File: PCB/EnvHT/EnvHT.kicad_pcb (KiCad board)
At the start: 2 copper layers, 29.5 x 18.4 mm, 21 parts, among them J1 DC, J2 DC, J4 Shelly, U1 LMR16006XDDCR, U4 ESP32-PICO-MINI-02, U7 SHT40

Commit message: Library update
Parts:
- added C5: 10nF, RevK:C_0603, F.Cu at (88.7, 88.8)
- added S1: Screw, RevK:Screw, F.Cu at (81.0, 84.0)
- added S2: Screw, RevK:Screw, F.Cu at (124.0, 84.0)
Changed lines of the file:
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@@
   (net 39 "unconnected-(U1-Pad1)")
   (net 40 "unconnected-(U1-Pad6)")
+  (footprint "RevK:C_0603" (layer "F.Cu")
+    (at 88.7 88.75 -90)
+    (descr "Capacitor SMD 0603 (1608 Metric), square (rectangular) end terminal, IPC_7351 nominal, (Body size source: IPC-SM-782 page 76, https://www.pcb-3d.com/wordpress/wp-content/uploads/ipc-sm-782a_amendment_1_and_2.pdf), generated with kicad-footprint-generator")
+    (tags "capacitor")
+    (property "Sheetfile" "EnvHT.kicad_sch")
+    (property "Sheetname" "")
+    (attr smd)
+    (fp_text reference "C5" (at -1.6 0) (layer "F.SilkS") hide
+      (effects (font (size 0.5 0.5) (thickness 0.08)))
+    )
+    (fp_text value "10nF" (at 0 0 90) (layer "F.Fab")
+      (effects (font (size 0.4 0.4) (thickness 0.08)))
+    )
+    (fp_text user "${REFERENCE}" (at 0 -0.8 90) (layer "F.Fab")
+      (effects (font (size 0.4 0.4) (thickness 0.06)))
+    )
+    (fp_line (start -0.3 -0.5) (end 0.3 -0.5) (layer "F.SilkS") (width 0.12))
+    (fp_line (start -0.3 0.5) (end 0.3 0.5) (layer "F.SilkS") (width 0.12))
+    (fp_line (start -0.8 0.4) (end -0.8 -0.4) (layer "F.CrtYd") (width 0.05))
+    (fp_line (start -0.8 -0.4) (end 0.8 -0.4) (layer "F.CrtYd") (width 0.05))
+    (fp_line (start 0.8 0.4) (end -0.8 0.4) (layer "F.CrtYd") (width 0.05))
+    (fp_line (start 0.8 -0.4) (end 0.8 0.4) (layer "F.CrtYd") (width 0.05))
+    (fp_line (start -0.8 0.4) (end -0.8 -0.4) (layer "F.Fab") (width 0.1))
+    (fp_line (start 0.8 -0.4) (end 0.8 0.4) (layer "F.Fab") (width 0.1))
+    (fp_line (start -0.8 -0.4) (end 0.8 -0.4) (layer "F.Fab") (width 0.1))
+    (fp_line (start 0.8 0.4) (end -0.8 0.4) (layer "F.Fab") (width 0.1))
+    (pad "1" smd roundrect (at -0.775 0 270) (size 0.8 0.95) (layers "F.Cu" "F.Paste" "F.Mask") (roundrect_rratio 0.25)
+      (net 5 "GND") (pintype "passive"))
+    (pad "2" smd roundrect (at 0.775 0 270) (size 0.8 0.95) (layers "F.Cu" "F.Paste" "F.Mask") (roundrect_rratio 0.25)
+      (net 2 "Net-(R12-Pad2)") (pintype "passive"))
+    (model "${KICAD6_3DMODEL_DIR}/Capacitor_SMD.3dshapes/C_0603_1608Metric.step"
+      (offset (xyz 0 0 0))
+      (scale (xyz 1 1 1))
+      (rotate (xyz 0 0 0))
+    )
+  )
   (footprint "RevK:R_0603" (layer "F.Cu")
     (at 106.925 88.75)
@@
     )
   )
+  (footprint "RevK:Screw" (layer "F.Cu")
+    (at 81 84)
+    (property "Sheetfile" "EnvHT.kicad_sch")
+    (property "Sheetname" "")
+    (property "exclude_from_bom" "")
+    (attr exclude_from_bom)
+    (fp_text reference "S1" (at 0.15 -2.65 unlocked) (layer "F.SilkS") hide
+      (effects (font (size 1 1) (thickness 0.15)))
+    )
+    (fp_text value "Screw" (at 0.05 4 unlocked) (layer "F.Fab")
+      (effects (font (size 1 1) (thickness 0.15)))
+    )
+    (fp_line (start -3 0) (end 3 0) (layer "F.Fab") (width 1))
+    (fp_line (start 0 -3) (end 0 3) (layer "F.Fab") (width 1))
+    (fp_circle (center 0 0) (end 6 0) (layer "F.Fab") (width 0.1) (fill none))
+    (model "/Users/adrian/Documents/KiCad/3D/653612.stp"
+      (offset (xyz 0 0 5))
+      (scale (xyz 1 1 1))
+      (rotate (xyz 0 90 0))
+    )
+  )
   (footprint "RevK:C_0603_" (layer "F.Cu")
     (at 107.95 87.3)
@@
     )
   )
+  (footprint "RevK:Screw" (layer "F.Cu")
+    (at 124 84)
+    (property "Sheetfile" "EnvHT.kicad_sch")
+    (property "Sheetname" "")
+    (property "exclude_from_bom" "")
+    (attr exclude_from_bom)
+    (fp_text reference "S2" (at 0.15 -2.65 unlocked) (layer "F.SilkS") hide
+      (effects (font (size 1 1) (thickness 0.15)))
+    )
+    (fp_text value "Screw" (at 0.05 4 unlocked) (layer "F.Fab")
+      (effects (font (size 1 1) (thickness 0.15)))
+    )
+    (fp_line (start -3 0) (end 3 0) (layer "F.Fab") (width 1))
+    (fp_line (start 0 -3) (end 0 3) (layer "F.Fab") (width 1))
+    (fp_circle (center 0 0) (end 6 0) (layer "F.Fab") (width 0.1) (fill none))
+    (model "/Users/adrian/Documents/KiCad/3D/653612.stp"
+      (offset (xyz 0 0 5))
+      (scale (xyz 1 1 1))
+      (rotate (xyz 0 90 0))
+    )
+  )

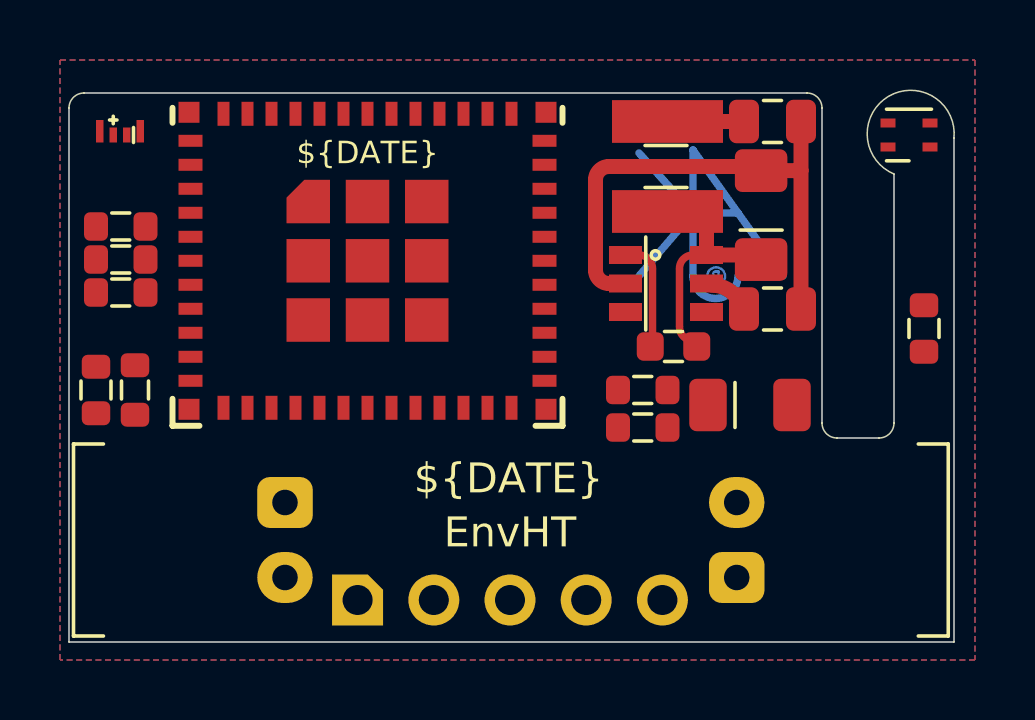
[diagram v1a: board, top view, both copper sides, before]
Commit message: Tracked EnvHT
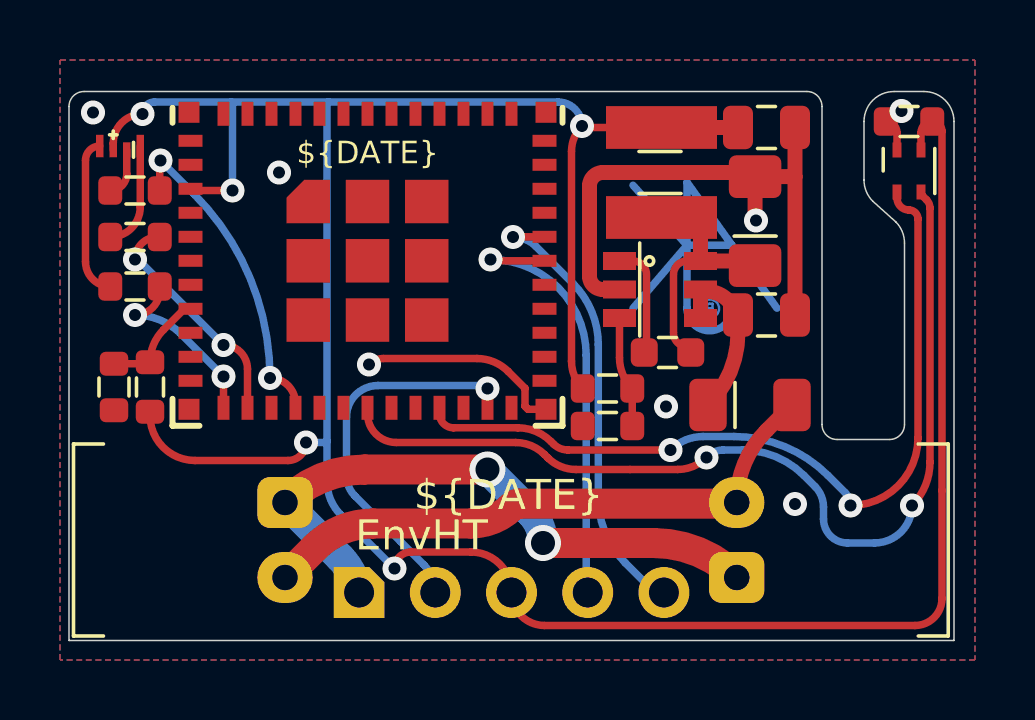
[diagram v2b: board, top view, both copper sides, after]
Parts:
- moved C4 6.92 mm to (115.8, 79.8), turned to 180 degrees
- moved R7 2.35 mm to (90.0, 82.1)
- moved U7 1.20 mm to (115.8, 81.5), turned to 90 degrees
- moved R1 1.18 mm to (105.8, 88.7)
- moved R2 1.18 mm to (105.8, 90.0)
- moved Logo1 1.09 mm to (108.4, 83.9)
- moved C5 0.61 mm to (89.3, 88.7), turned to 90 degrees
- moved R8 0.59 mm to (90.0, 83.7)
- moved R9 0.52 mm to (90.0, 85.3)
- moved R12 0.51 mm to (90.5, 88.7), turned to 90 degrees
- moved D3 0.49 mm to (89.5, 80.7)
- moved C1 0.28 mm to (107.8, 87.5)
- moved C2 0.28 mm to (111.0, 86.2)
- moved C3 0.28 mm to (111.0, 80.0)
- moved D1 0.28 mm to (110.7, 83.1)
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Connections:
- U4 pad 12: unconnected-(U4-Pad12) -> B
- U4 pad 13: unconnected-(U4-Pad13) -> G
- U4 pad 15: unconnected-(U4-Pad15) -> R
- U4 pad 18: unconnected-(U4-Pad18) -> SCL
- U4 pad 21: unconnected-(U4-Pad21) -> SDA
- U4 pad 27: G -> unconnected-(U4-Pad27)
- U4 pad 28: R -> unconnected-(U4-Pad28)
- U4 pad 33: B -> unconnected-(U4-Pad33)
- U4 pad 34: SDA -> unconnected-(U4-Pad34)
- U4 pad 35: SCL -> unconnected-(U4-Pad35)
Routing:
- net +3.3V: track 0.00 -> 94.2 mm, vias 0 -> 5
- net SCL: track 0.00 -> 32.3 mm, vias 0 -> 2
- net GND: track 0.00 -> 30.6 mm, vias 0 -> 9
- net SDA: track 0.00 -> 27.3 mm, vias 0 -> 2
- net Net-(D2-Pad2): track 0.00 -> 19.7 mm
- net O: track 0.00 -> 15.1 mm, vias 0 -> 1
- net I: track 0.00 -> 14.9 mm, vias 0 -> 1
- net BOOT: track 0.00 -> 12.9 mm, vias 0 -> 1
- net R: track 0.00 -> 10.8 mm, vias 0 -> 2
- net G: track 0.00 -> 7.86 mm, vias 0 -> 2
- net B: track 0.00 -> 6.13 mm, vias 0 -> 2
- net Net-(D3-Pad1): track 0.00 -> 5.37 mm
- net DC: track 0.00 -> 4.20 mm
- net Net-(R1-Pad2): track 0.00 -> 3.71 mm
- net Net-(C5-Pad2): track 0.00 -> 3.60 mm
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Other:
- board size 29.5 x 18.4 mm -> 29.5 x 18.3 mm

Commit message: Library update
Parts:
- moved S1 2.00 mm to (83.0, 84.0)
- moved S2 2.00 mm to (122.0, 84.0)

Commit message: Tody
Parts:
- moved S1 1.00 mm to (84.0, 84.0)
- moved S2 1.00 mm to (121.0, 84.0)
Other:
- board size 29.5 x 18.3 mm -> 29.5 x 18.2 mm
- board text added: "SDA: 15 SCL: 14"
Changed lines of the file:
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@@
     )
   )
-  (property "DATE" "2023-04-29")
+  (property "DATE" "2023-05-01")
   (net 0 "")
   (net 1 "Net-(D2-Pad2)")
@@
   )
   (footprint "RevK:Screw" (layer "F.Cu")
-    (at 83 84)
+    (at 84 84)
     (property "Sheetfile" "EnvHT.kicad_sch")
     (property "Sheetname" "")
@@
   )
   (footprint "RevK:Screw" (layer "F.Cu")
-    (at 122 84)
+    (at 121 84)
     (property "Sheetfile" "EnvHT.kicad_sch")
     (property "Sheetname" "")
@@
       (effects (font (size 0.5 0.5) (thickness 0.08)) (justify mirror))
     )
-    (fp_text user "3.3" (at -0.7 0.7 315 unlocked) (layer "B.SilkS")
-      (effects (font (size 0.7 0.7) (thickness 0.1)) (justify mirror))
-    )
     (fp_text user "3V3" (at -0.83 0.8 315 unlocked) (layer "B.SilkS")
       (effects (font (size 0.5 0.5) (thickness 0.08)) (justify mirror))
@@
       (net 20 "O") (pinfunction "Tx") (pintype "passive"))
   )
-  (gr_line (start 127.8 78) (end 77.2 78) (layer "Eco1.User") (width 0.1))
-  (gr_line (start 77.2 97.1) (end 127.8 97.1) (layer "Eco1.User") (width 0.1))
-  (gr_line (start 77.2 78) (end 77.2 97.1) (layer "Eco1.User") (width 0.1))
-  (gr_line (start 127.8 97.1) (end 127.8 78) (layer "Eco1.User") (width 0.1))
+  (gr_line (start 124 77) (end 81 77) (layer "Eco1.User") (width 0.1))
+  (gr_arc (start 81 97) (mid 80.292893 96.707107) (end 80 96) (layer "Eco1.User") (width 0.1))
+  (gr_arc (start 125 96) (mid 124.707107 96.707107) (end 124 97) (layer "Eco1.User") (width 0.1))
+  (gr_line (start 81 97) (end 124 97) (layer "Eco1.User") (width 0.1))
+  (gr_line (start 80 78) (end 80 96) (layer "Eco1.User") (width 0.1))
+  (gr_line (start 125 96) (end 125 78) (layer "Eco1.User") (width 0.1))
+  (gr_arc (start 124 77) (mid 124.707107 77.292893) (end 125 78) (layer "Eco1.User") (width 0.1))
+  (gr_arc (start 80 78) (mid 80.292893 77.292893) (end 81 77) (layer "Eco1.User") (width 0.1))
   (gr_line (start 116.3 78.8) (end 115.3 78.8) (layer "Edge.Cuts") (width 0.05))
   (gr_line (start 114.3 79.8) (end 114.3 81.75) (layer "Edge.Cuts") (width 0.05))
-  (gr_line (start 117.3 97.1) (end 117.3 79.8) (layer "Edge.Cuts") (width 0.05))
+  (gr_line (start 117.3 97) (end 117.3 79.8) (layer "Edge.Cuts") (width 0.05))
   (gr_line (start 115.65 83.85) (end 115.65 89.9) (layer "Edge.Cuts") (width 0.05))
   (gr_arc (start 115.65 89.9) (mid 115.503553 90.253553) (end 115.15 90.4) (layer "Edge.Cuts") (width 0.05))
@@
   (gr_arc (start 112.4 78.8) (mid 112.753553 78.946447) (end 112.9 79.3) (layer "Edge.Cuts") (width 0.05))
   (gr_arc (start 114.592893 82.457107) (mid 114.37612 82.132684) (end 114.3 81.75) (layer "Edge.Cuts") (width 0.05))
-  (gr_line (start 87.8 97.1) (end 117.3 97.1) (layer "Edge.Cuts") (width 0.05))
-  (gr_line (start 87.8 97.1) (end 87.8 79.3) (layer "Edge.Cuts") (width 0.05))
+  (gr_line (start 87.8 97) (end 117.3 97) (layer "Edge.Cuts") (width 0.05))
+  (gr_line (start 87.8 97) (end 87.8 79.3) (layer "Edge.Cuts") (width 0.05))
   (gr_arc (start 114.3 79.8) (mid 114.592893 79.092893) (end 115.3 78.8) (layer "Edge.Cuts") (width 0.05))
   (gr_line (start 112.9 79.3) (end 112.9 89.9) (layer "Edge.Cuts") (width 0.05))
   (gr_line (start 88.3 78.8) (end 112.4 78.8) (layer "Edge.Cuts") (width 0.05))
+  (gr_text "SDA: 15\nSCL: 14" (at 98 84) (layer "B.SilkS")
+    (effects (font (size 1 1) (thickness 0.15)) (justify mirror))
+  )
   (gr_text "⏚" (at 112.1 95 90) (layer "B.SilkS")
     (effects (font (size 1 1) (thickness 0.15)) (justify mirror))
   )
-  (gr_text "12V" (at 112.8 92.5 180) (layer "B.SilkS")
+  (gr_text "12V" (at 107.5 92.5) (layer "B.SilkS")
     (effects (font (size 1 1) (thickness 0.15)) (justify mirror))
   )
@@
     (effects (font (size 1 1) (thickness 0.15)) (justify mirror))
   )
-  (gr_text "H/T" (at 115.9 80.2) (layer "B.SilkS")
+  (gr_text "H/T" (at 115.9 81) (layer "B.SilkS")
     (effects (font (size 0.75 0.75) (thickness 0.15)) (justify mirror))
   )
